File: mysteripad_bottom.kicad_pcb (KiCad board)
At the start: 2 copper layers, 76.2 x 146.6 mm, 9 parts, among them M8 MountingHole_4.3mm_M4_Pad

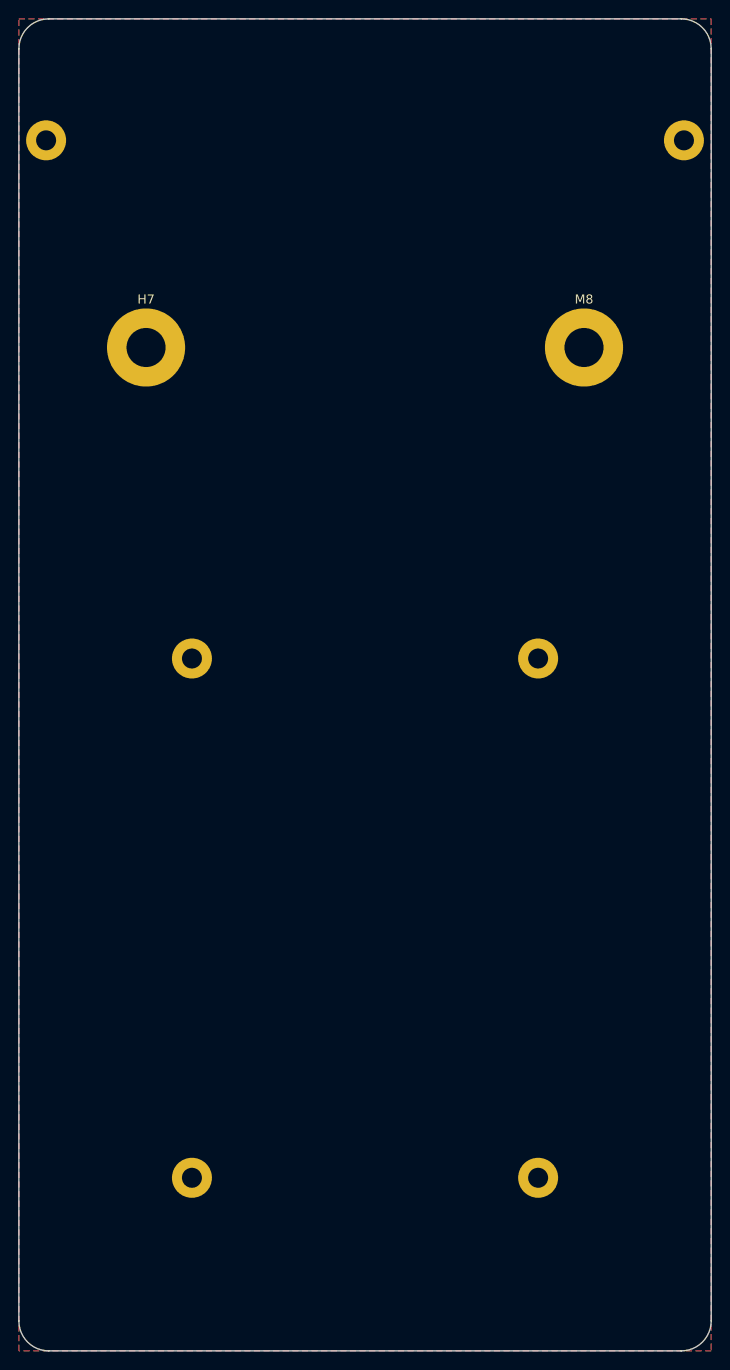
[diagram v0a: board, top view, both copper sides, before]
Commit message: Fix incorrect USB pullup; fix bottom mounting holes
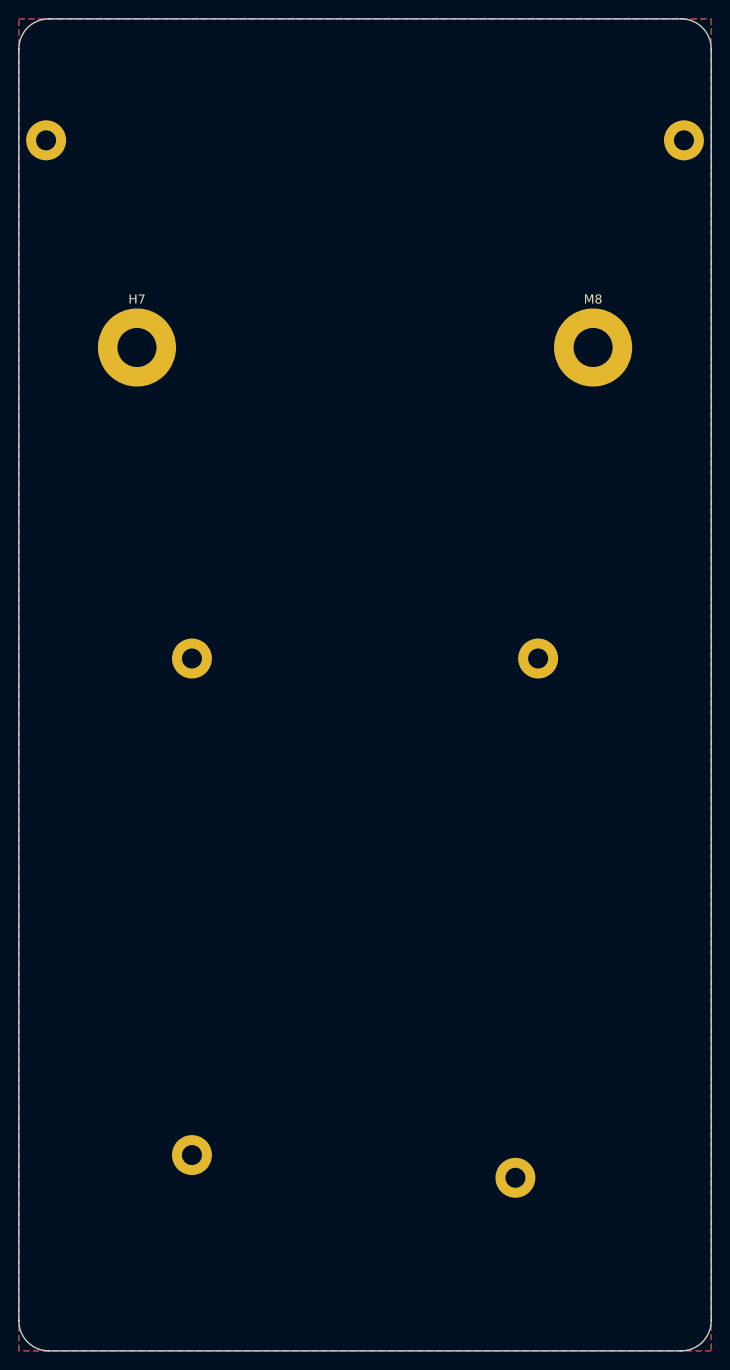
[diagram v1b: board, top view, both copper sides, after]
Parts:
- moved H5 2.50 mm to (89.1, 155.1)
- moved H6 2.50 mm to (124.7, 157.6)
- moved H7 1.00 mm to (83.0, 66.2)
- moved M8 1.00 mm to (133.2, 66.2)
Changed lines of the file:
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@@
       (usegerberextensions false)
       (usegerberattributes true)
-      (usegerberadvancedattributes true)
+      (usegerberadvancedattributes false)
       (creategerberjobfile true)
       (svguseinch false)
@@
       (outputformat 1)
       (mirror false)
-      (drillshape 1)
+      (drillshape 0)
       (scaleselection 1)
-      (outputdirectory "")
+      (outputdirectory "Gerbers/bottom")
     )
   )
@@
   )
   (footprint "MountingHole:MountingHole_2.2mm_M2_Pad" (layer "F.Cu")
-    (at 89.05006 157.55)
+    (at 89.05006 155.05)
     (descr "Mounting Hole 2.2mm, M2")
     (tags "mounting hole 2.2mm m2")
@@
   )
   (footprint "MountingHole:MountingHole_4.3mm_M4_Pad" (layer "F.Cu")
-    (at 84 66.17)
+    (at 83 66.17)
     (descr "Mounting Hole 4.3mm, M4")
     (tags "mounting hole 4.3mm m4")
@@
   )
   (footprint "MountingHole:MountingHole_2.2mm_M2_Pad" (layer "F.Cu")
-    (at 127.15006 157.55)
+    (at 124.65006 157.55)
     (descr "Mounting Hole 2.2mm, M2")
     (tags "mounting hole 2.2mm m2")
@@
   )
   (footprint "MountingHole:MountingHole_4.3mm_M4_Pad" (layer "F.Cu")
-    (at 132.2 66.17)
+    (at 133.2 66.17)
     (descr "Mounting Hole 4.3mm, M4")
     (tags "mounting hole 4.3mm m4")
@@
   (gr_arc (start 146.2 173.3) (mid 145.233452 175.633452) (end 142.9 176.6) (layer "Edge.Cuts") (width 0.15))
   (gr_line (start 142.9 30) (end 73.3 30) (layer "Edge.Cuts") (width 0.15))
-  (gr_circle (center 84 66.17) (end 94.900041 66.17) (layer "F.CrtYd") (width 0.1) (fill none))
-  (gr_circle (center 132.2 66.17) (end 143.100041 66.17) (layer "F.CrtYd") (width 0.1) (fill none))
+  (gr_circle (center 83 66.17) (end 93.900041 66.17) (layer "F.CrtYd") (width 0.1) (fill none))
+  (gr_circle (center 133.2 66.17) (end 144.100041 66.17) (layer "F.CrtYd") (width 0.1) (fill none))
   (gr_text "MYSTERIPAD" (at 108 87.7) (layer "F.Mask")
     (effects (font (size 5 5.4) (thickness 0.8)))
   )
-  (gr_text "42keebs.eu" (at 108.2 93.1) (layer "F.Mask")
-    (effects (font (size 1 1) (thickness 0.15)))
+  (gr_text "42keebs.eu" (at 108.2 92.95) (layer "F.Mask")
+    (effects (font (size 1.2 1.2) (thickness 0.2)))
   )
   (zone (net 0) (net_name "") (layers F&B.Cu) (hatch edge 0.508)
@@
     )
   )
-  (group "" (id 5edd5b7d-ab54-4755-9eae-f42c9666c0ad)
+  (group "" (id a38c111a-7915-4c42-b1d9-1ed698024f43)
     (members
       39528bf6-b5a9-4e57-a762-7925b99ba07e
